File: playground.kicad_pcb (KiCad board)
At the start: 4 copper layers, 80.5 x 50.5 mm, 74 parts, among them IC1 TXU0101DBVR, IC11 LM3940IMP-3.3_NOPB, IC2 TXU0101DBVR, IC3 TXU0101DBVR, IC4 TXU0101DBVR, IC5 TXU0101DBVR, IC6 TXU0101DBVR, IC7 TXU0101DBVR, IC8 TXU0101DBVR, IC9 L293DD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

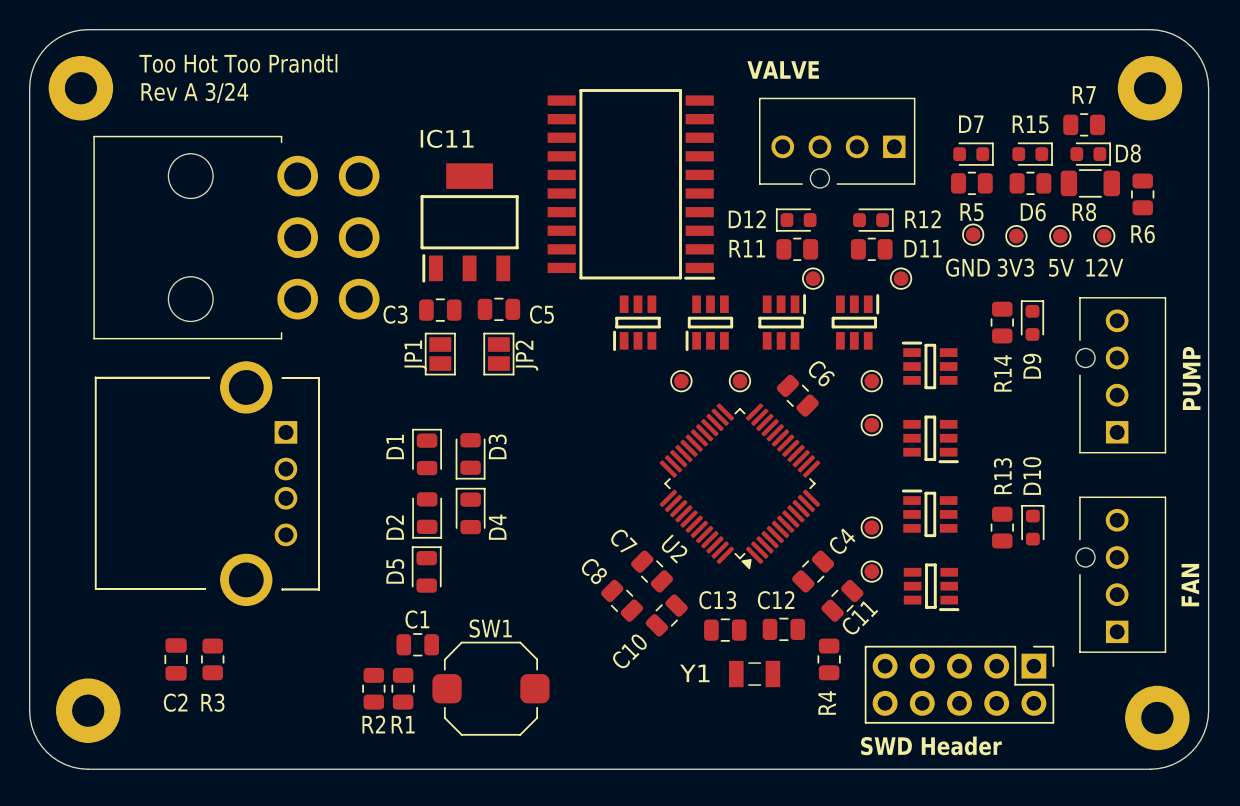
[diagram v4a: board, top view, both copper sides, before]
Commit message: Fixed board outline
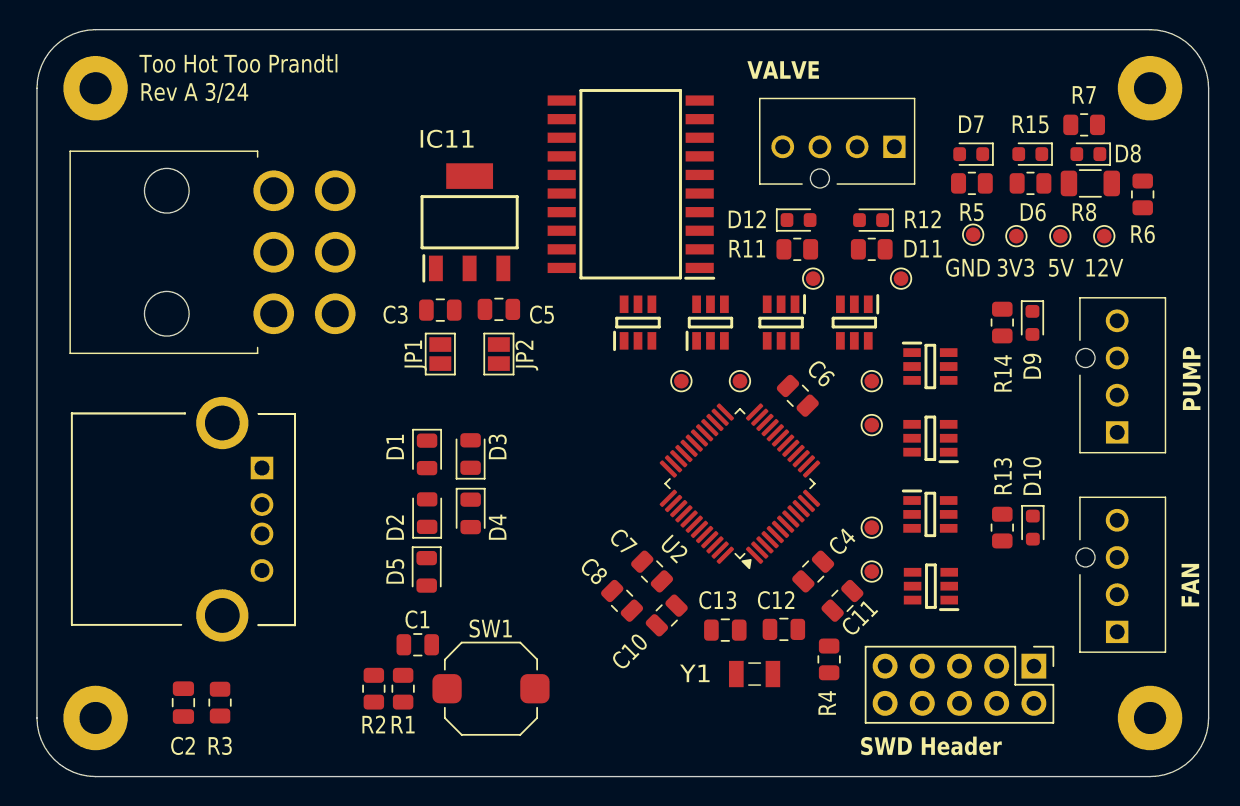
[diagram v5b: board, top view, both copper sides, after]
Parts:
- moved C2 2.99 mm to (92.0, 104.9)
- moved R3 2.99 mm to (94.5, 104.9)
- moved J1 2.93 mm to (97.4, 88.9)
- moved J6 1.92 mm to (98.2, 78.4)
- moved H3 1.00 mm to (86.0, 63.0)
- moved H2 0.50 mm to (158.0, 106.0)
- moved H4 0.50 mm to (86.0, 105.5)
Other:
- board size 80.5 x 50.5 mm -> 80 x 51 mm
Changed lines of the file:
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@@
 	(footprint "custom_footprints:676432910"
 		(layer "F.Cu")
-		(at 99 86.5 -90)
+		(at 97.365 88.93 -90)
 		(descr "67643-2910-2")
 		(tags "Connector")
@@
 		(tags "resistor")
 		(property "Reference" "R13"
-			(at 3.5 0.0875 270)
+			(at 3.5 0.0875 -90)
 			(layer "F.SilkS")
 			(effects
@@
 		)
 		(property "Value" "20R"
-			(at 0 1.65 270)
+			(at 0 1.65 -90)
 			(layer "F.Fab")
 			(effects
@@
 		)
 		(fp_text user "${REFERENCE}"
-			(at 0 0 270)
+			(at 0 0 -90)
 			(layer "F.Fab")
 			(effects
@@
 		(tags "resistor")
 		(property "Reference" "R14"
-			(at -3.5 0.0875 270)
+			(at -3.5 0.0875 -90)
 			(layer "F.SilkS")
 			(effects
@@
 		)
 		(property "Value" "20R"
-			(at 0 1.65 270)
+			(at 0 1.65 -90)
 			(layer "F.Fab")
 			(effects
@@
 		)
 		(fp_text user "${REFERENCE}"
-			(at 0 0 270)
+			(at 0 0 -90)
 			(layer "F.Fab")
 			(effects
@@
 	(footprint "MountingHole:MountingHole_2.2mm_M2_Pad"
 		(layer "F.Cu")
-		(at 158.5 106)
+		(at 158 106)
 		(descr "Mounting Hole 2.2mm, M2")
 		(tags "mounting hole 2.2mm m2")
@@
 	(footprint "MountingHole:MountingHole_2.2mm_M2_Pad"
 		(layer "F.Cu")
-		(at 85 63)
+		(at 86 63)
 		(descr "Mounting Hole 2.2mm, M2")
 		(tags "mounting hole 2.2mm m2")
@@
 		(tags "resistor")
 		(property "Reference" "R5"
-			(at 0 2.000001 360)
+			(at 0 2.000001 0)
 			(layer "F.SilkS")
 			(effects
@@
 		)
 		(property "Value" "51R"
-			(at 0 1.65 360)
+			(at 0 1.65 0)
 			(layer "F.Fab")
 			(effects
@@
 		)
 		(fp_text user "${REFERENCE}"
-			(at 0 0 360)
+			(at 0 0 0)
 			(layer "F.Fab")
 			(effects
@@
 	(footprint "custom_footprints:455580003"
 		(layer "F.Cu")
-		(at 99.8 77.399999 90)
+		(at 98.165 78.399999 90)
 		(descr "45558-0003-3")
 		(tags "Connector")
@@
 	(footprint "Capacitor_SMD:C_0805_2012Metric"
 		(layer "F.Cu")
-		(at 91.5 102 -90)
+		(at 92 104.949999 -90)
 		(descr "Capacitor SMD 0805 (2012 Metric), square (rectangular) end terminal, IPC_7351 nominal, (Body size source: IPC-SM-782 page 76, https://www.pcb-3d.com/wordpress/wp-content/uploads/ipc-sm-782a_amendment_1_and_2.pdf, https://docs.google.com/spreadsheets/d/1BsfQQcO9C6DZCsRaXUlFlo91Tg2WpOkGARC1WS5S8t0/edit?usp=sharing), generated with kicad-footprint-generator")
 		(tags "capacitor")
@@
 		(tags "resistor")
 		(property "Reference" "R7"
-			(at 0 -2 360)
+			(at 0 -2 0)
 			(layer "F.SilkS")
 			(effects
@@
 		)
 		(property "Value" "470R"
-			(at 0 1.65 360)
+			(at 0 1.65 0)
 			(layer "F.Fab")
 			(effects
@@
 		)
 		(fp_text user "${REFERENCE}"
-			(at 0 0 360)
+			(at 0 0 0)
 			(layer "F.Fab")
 			(effects
@@
 	(footprint "MountingHole:MountingHole_2.2mm_M2_Pad"
 		(layer "F.Cu")
-		(at 85.5 105.5)
+		(at 86 105.5)
 		(descr "Mounting Hole 2.2mm, M2")
 		(tags "mounting hole 2.2mm m2")
@@
 		)
 		(pad "1" thru_hole circle
-			(at 0 0)
+			(at 0 0.5)
 			(size 4.4 4.4)
 			(drill 2.2)
@@
 	(footprint "Resistor_SMD:R_0805_2012Metric"
 		(layer "F.Cu")
-		(at 94.000001 102 -90)
+		(at 94.500001 104.949999 -90)
 		(descr "Resistor SMD 0805 (2012 Metric), square (rectangular) end terminal, IPC_7351 nominal, (Body size source: IPC-SM-782 page 72, https://www.pcb-3d.com/wordpress/wp-content/uploads/ipc-sm-782a_amendment_1_and_2.pdf), generated with kicad-footprint-generator")
 		(tags "resistor")
@@
 		(tags "resistor")
 		(property "Reference" "R12"
-			(at 3.5 -2 360)
+			(at 3.5 -2 0)
 			(layer "F.SilkS")
 			(effects
@@
 		)
 		(property "Value" "20R"
-			(at 0 1.65 360)
+			(at 0 1.65 0)
 			(layer "F.Fab")
 			(effects
@@
 		)
 		(fp_text user "${REFERENCE}"
-			(at 0 0 360)
+			(at 0 0 0)
 			(layer "F.Fab")
 			(effects
@@
 	)
 	(gr_arc
-		(start 158 59)
-		(mid 160.828427 60.171573)
-		(end 162 63)
+		(start 82 63)
+		(mid 83.171573 60.171573)
+		(end 86 59)
 		(stroke
 			(width 0.05)
@@
 		(layer "Edge.Cuts")
 	)
-	(gr_arc
-		(start 162 105.5)
-		(mid 160.828427 108.328427)
-		(end 158 109.5)
+	(gr_line
+		(start 162 106)
+		(end 162 63)
 		(stroke
 			(width 0.05)
@@
 	)
 	(gr_arc
-		(start 81.5 63)
-		(mid 82.671573 60.171573)
-		(end 85.5 59)
+		(start 162 106)
+		(mid 160.828427 108.828427)
+		(end 158 110)
 		(stroke
 			(width 0.05)
@@
 		(layer "Edge.Cuts")
 	)
-	(gr_line
-		(start 81.5 105.5)
-		(end 81.5 63)
+	(gr_arc
+		(start 158 59)
+		(mid 160.828427 60.171573)
+		(end 162 63)
 		(stroke
 			(width 0.05)
@@
 	)
 	(gr_line
-		(start 162 63)
-		(end 162 105.5)
+		(start 82 106)
+		(end 82 63)
 		(stroke
 			(width 0.05)
@@
 		(layer "Edge.Cuts")
 	)
-	(gr_arc
-		(start 85.5 109.5)
-		(mid 82.671573 108.328427)
-		(end 81.5 105.5)
+	(gr_line
+		(start 86 110)
+		(end 158 110)
 		(stroke
 			(width 0.05)
@@
 		(layer "Edge.Cuts")
 	)
-	(gr_line
-		(start 85.5 59)
-		(end 158 59)
+	(gr_arc
+		(start 86 110)
+		(mid 83.171573 108.828427)
+		(end 82 106)
 		(stroke
 			(width 0.05)
@@
 	)
 	(gr_line
-		(start 158 109.5)
-		(end 85.5 109.5)
+		(start 86 59)
+		(end 158 59)
 		(stroke
 			(width 0.05)

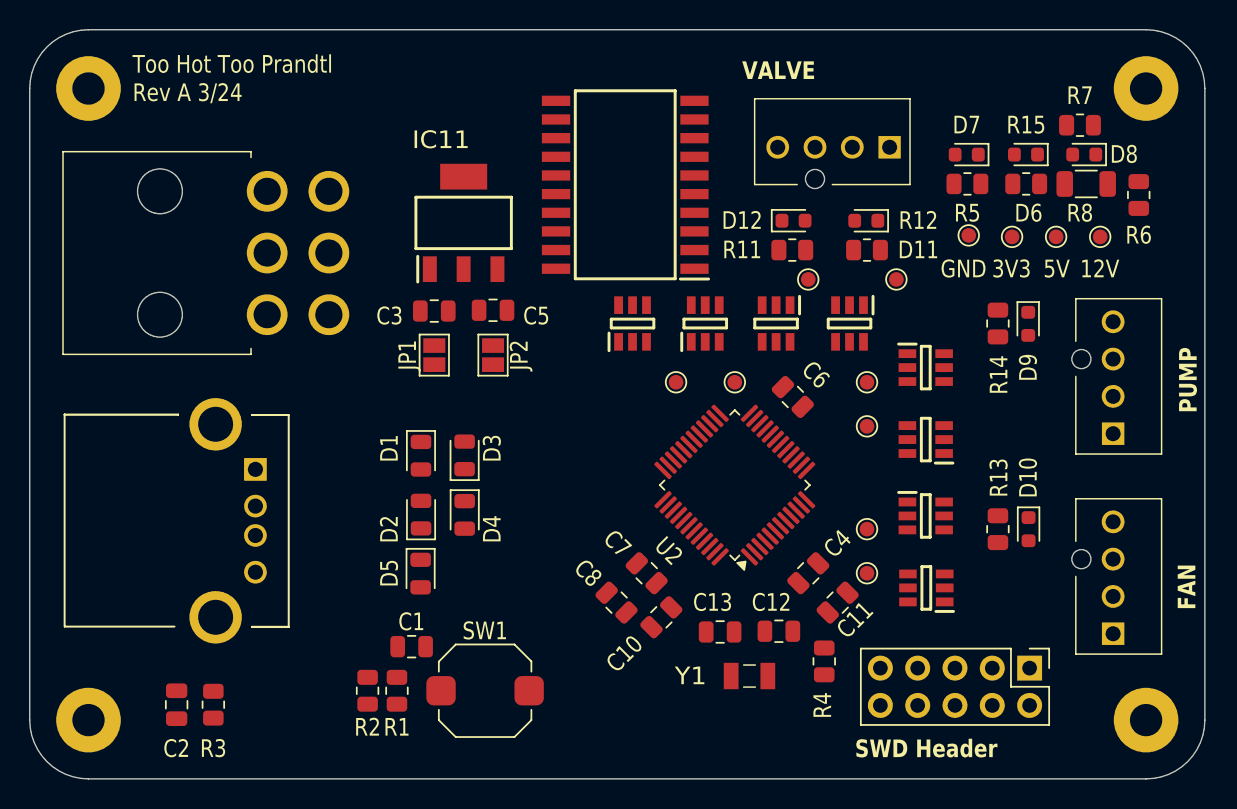
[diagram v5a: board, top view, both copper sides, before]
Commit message: Layout and Route of 4 layer version complete.
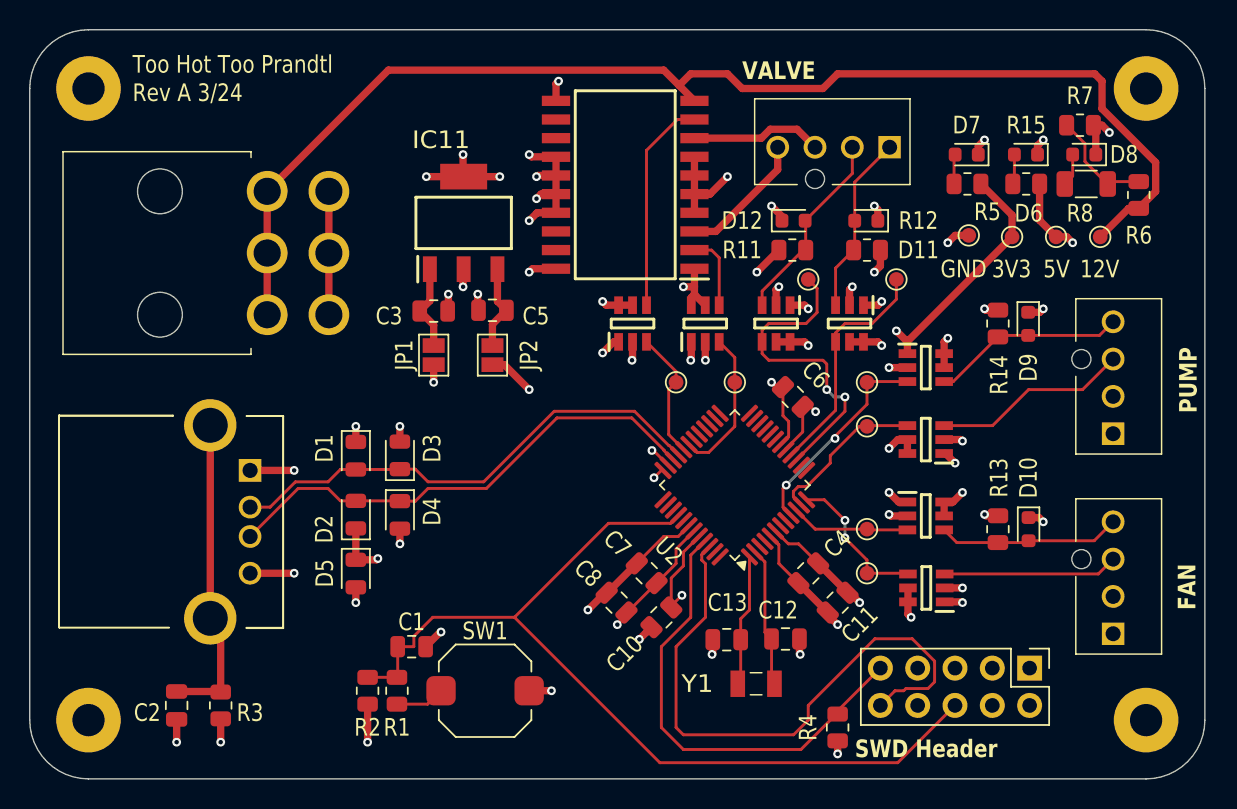
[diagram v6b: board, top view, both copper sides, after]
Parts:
- moved R4 4.59 mm to (137.0, 106.5)
- moved D2 4.44 mm to (104.2, 92.0)
- moved D1 4.44 mm to (104.2, 88.0)
- moved D4 4.41 mm to (107.2, 92.0)
- moved D5 4.41 mm to (104.2, 96.0)
- moved D3 4.41 mm to (107.2, 88.0)
- moved C13 0.69 mm to (129.4, 100.5)
- moved Y1 0.69 mm to (131.4, 103.5)
- moved C12 0.69 mm to (133.4, 100.5)
- moved R3 0.50 mm to (95.0, 105.0)
- moved H4 0.50 mm to (86.0, 106.0)
- moved J1 0.37 mm to (97.0, 89.0)
- moved C2 0.05 mm to (92.0, 105.0)
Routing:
- net GND: track 0.00 -> 92.8 mm, vias 0 -> 42
- net +12V: track 0.00 -> 86.0 mm
- net +3V3: track 0.00 -> 64.7 mm, vias 0 -> 16
- net /RESET: track 0.00 -> 63.1 mm
- net /SWDIO: track 0.00 -> 41.0 mm
- net +5V: track 0.00 -> 39.3 mm, vias 0 -> 19
- net /USB_D+: track 0.00 -> 34.1 mm
- net /USB_D-: track 0.00 -> 33.9 mm
- net /SWCLK: track 0.00 -> 31.8 mm
- net /ValveSense1_3v3: track 0.00 -> 21.9 mm, vias 0 -> 2
- net /usb_shield_gnd: track 0.00 -> 21.5 mm
- net /ValveSense2_3v3: track 0.00 -> 16.0 mm
- net /ValveCtrl2_5v: track 0.00 -> 14.7 mm
- net /PumpCtrl_3v3: track 0.00 -> 14.5 mm, vias 0 -> 2
- net /ValveSense1_5v: track 0.00 -> 13.4 mm
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- added copper zone on In2.Cu, net +3V3
- added copper zone on In2.Cu, net +5V
- added copper zone on In1.Cu, net GND

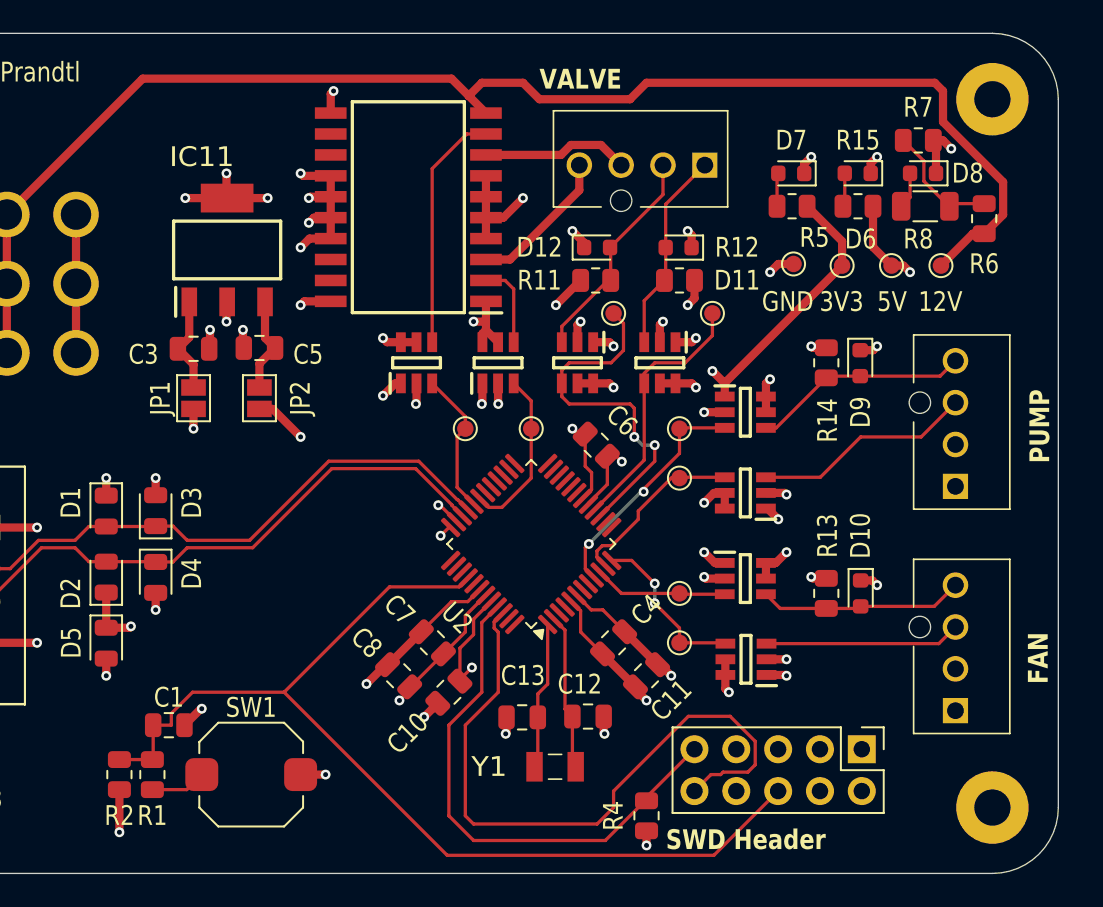
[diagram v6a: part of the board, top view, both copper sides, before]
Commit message: Modified layout. Added more silkscreen.
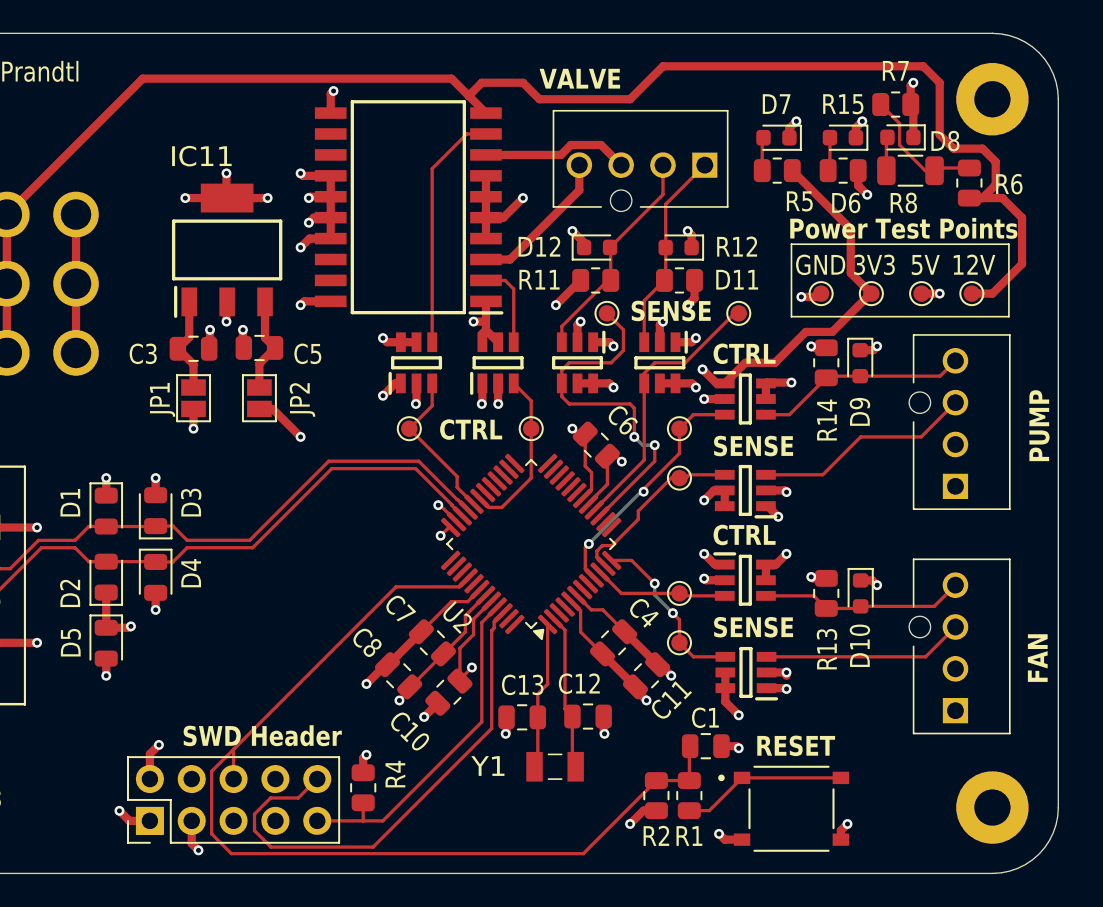
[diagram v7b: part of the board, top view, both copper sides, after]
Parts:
- removed SW1: SW_DIP_x01, Button_Switch_SMD:SW_Push_1TS009xxxx-xxxx-xxxx_6x6x5mm
- added S1: TS-1187A-B-A-B, custom_footprints:SW_TS-1187A-B-A-B, F.Cu at (145.8, 106.1)
- moved J5 43.4 mm to (106.8, 106.8), turned to 90 degrees
- moved C1 32.6 mm to (140.6, 102.3)
- moved R1 32.6 mm to (139.6, 105.3)
- moved R2 32.6 mm to (137.6, 105.3)
- moved R4 17.3 mm to (119.8, 104.8), turned to 90 degrees
- moved TP8 3.40 mm to (122.6, 83.0)
- moved D8 2.58 mm to (152.4, 65.3)
- moved R7 2.58 mm to (152.1, 63.3)
- moved TP1 2.53 mm to (156.8, 74.8), turned to -90 degrees
- moved TP2 2.49 mm to (153.7, 74.8), turned to -90 degrees
- moved TP4 2.46 mm to (147.6, 74.8), turned to -90 degrees
- moved TP3 2.46 mm to (150.7, 74.8), turned to -90 degrees
- moved D6 2.34 mm to (148.9, 65.3)
- moved R15 2.34 mm to (148.9, 67.3)
- moved R5 2.34 mm to (144.9, 67.3)
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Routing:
- net /SWCLK: track 31.8 -> 20.9 mm
- net /SWDIO: track 41.0 -> 30.8 mm
- net +3V3: track 64.7 -> 73.2 mm, vias 16 -> 17
- net +12V: track 86.0 -> 93.2 mm
- net /RST_SW_R: track 3.38 -> 10.0 mm
- net GND: track 92.8 -> 97.9 mm, vias 42 -> 45
- net /RESET: track 63.1 -> 59.5 mm
- net +5V: track 39.3 -> 37.1 mm, vias 19 -> 20
- net /ValveSense2_3v3: track 16.0 -> 16.8 mm
- net /ValveCtrl2_3v3: track 8.80 -> 9.54 mm
- net /LEDs/12v_PWD_LED_VOL_DIV: track 7.35 -> 7.88 mm
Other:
- board text added: "CTRL"
- board text added: "Power Test Points"
- board text added: "RESET"
- board text added: "SENSE"
